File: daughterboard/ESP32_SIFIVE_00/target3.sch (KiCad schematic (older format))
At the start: 0 parts

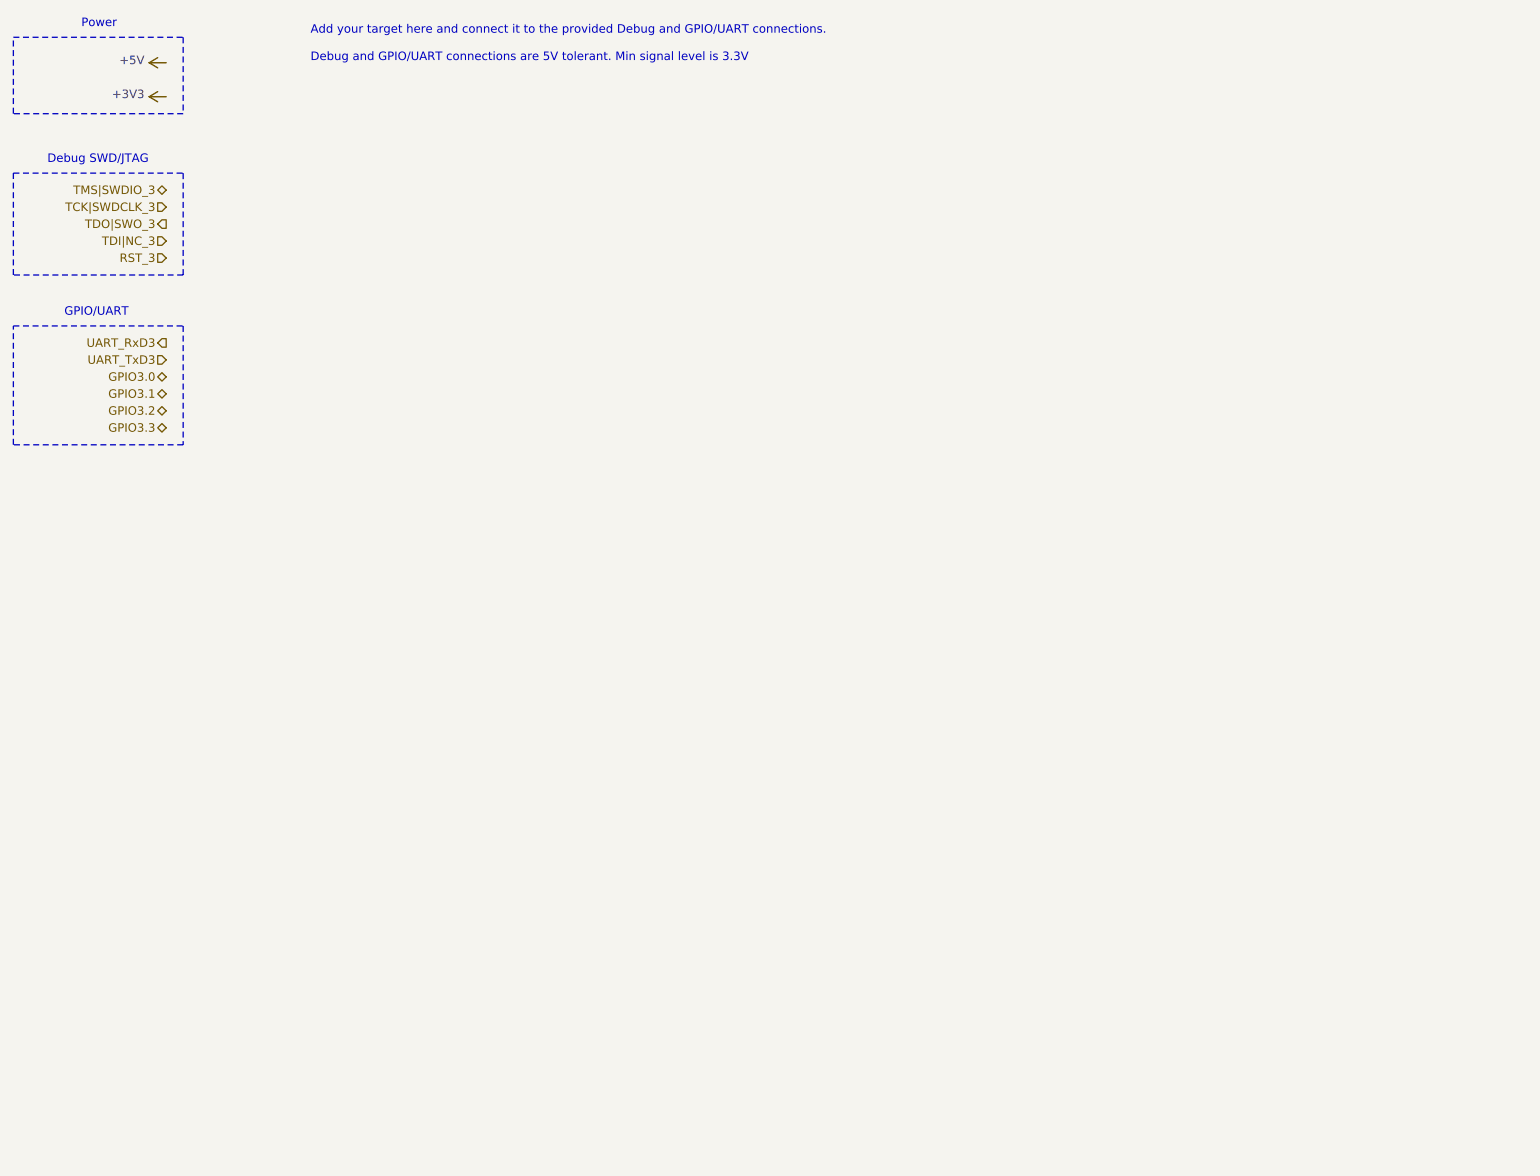
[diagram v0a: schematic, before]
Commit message: further work on ESP32/SIFIVE daughterboard
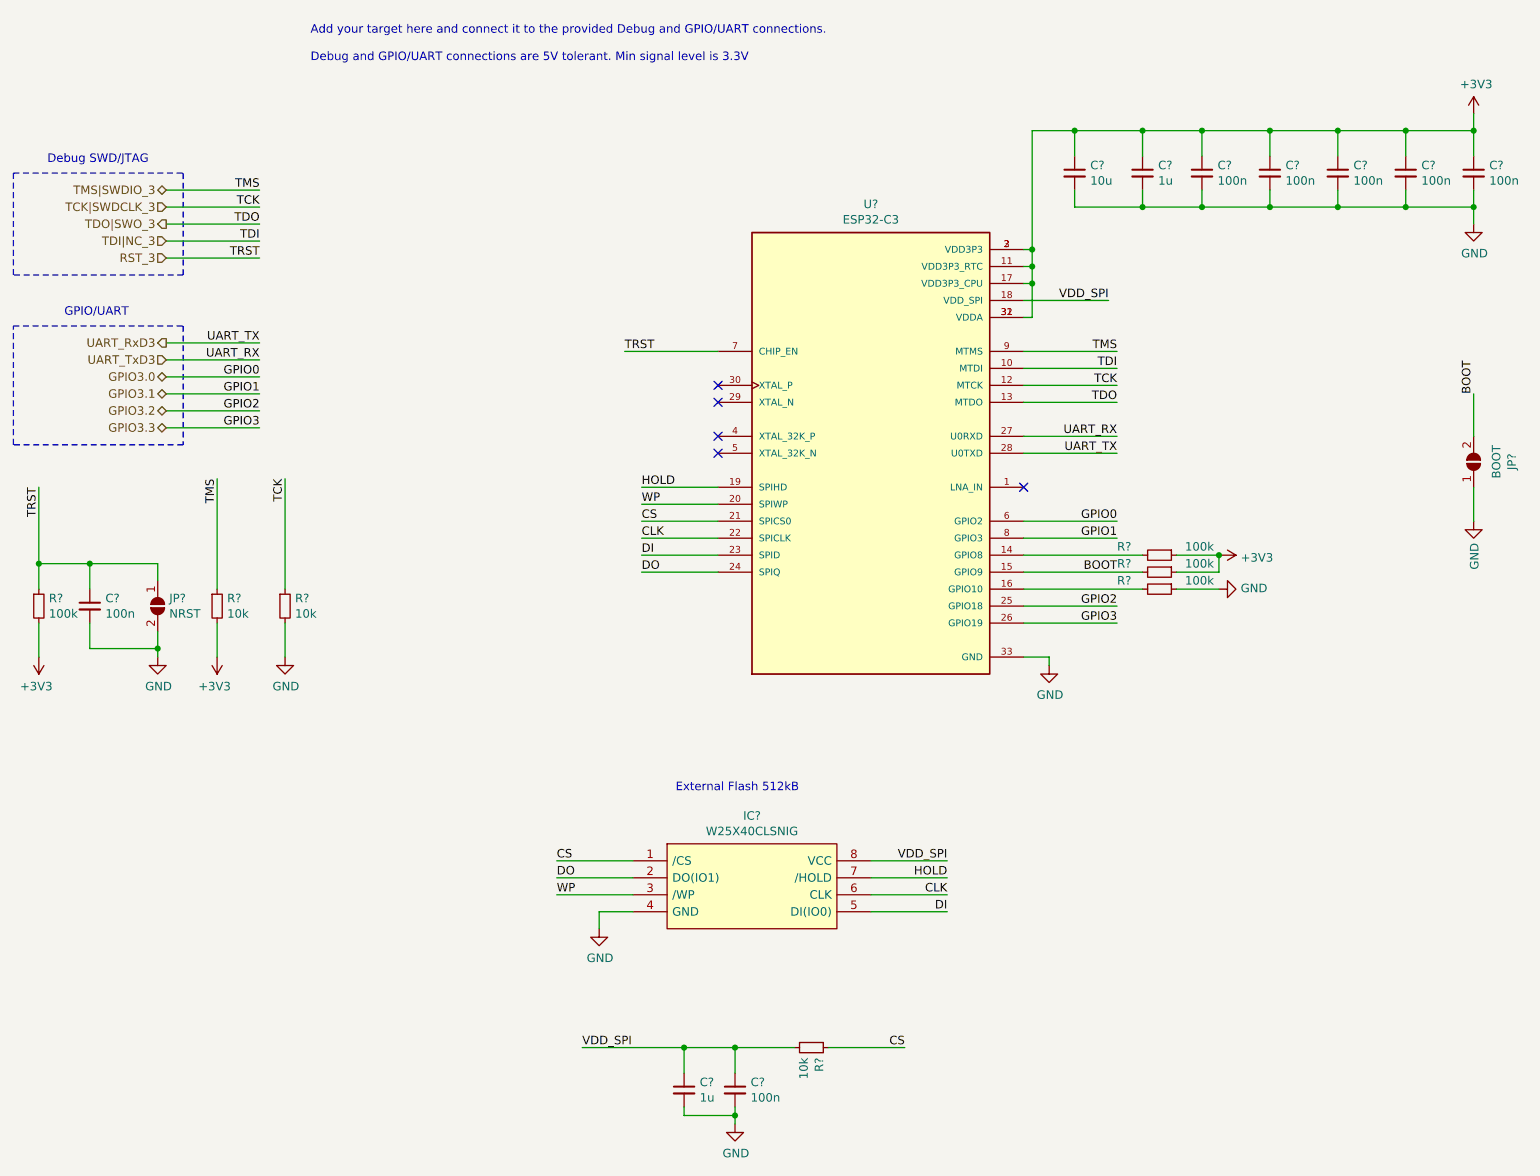
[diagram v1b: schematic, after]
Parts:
- added C? (x2): 1u, symbol Device:C_Small
- added C? (x7): 100n, symbol Device:C_Small
- added C?: 10u, symbol Device:C_Small
- added IC?: W25X40CLSNIG, hive_daughterboard:W25X40CLSNIG, symbol hive_daughterboard:W25X40CLSNIG
- added JP?: NRST, symbol Jumper:SolderJumper_2_Open
- added JP?: BOOT, symbol Jumper:SolderJumper_2_Open
- added R? (x3): 10k, symbol Device:R_Small
- added R? (x4): 100k, symbol Device:R_Small
- added U?: ESP32-C3, hive_daughterboard:ESP32-C3, symbol hive_daughterboard:ESP32-C3
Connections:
- net +3V3: now also C?.1, C?.1, C?.1, C?.1, C?.1, C?.1, C?.1, R?.1, R?.1, R?.2, R?.2, U?.11 (VDD3P3_RTC), U?.17 (VDD3P3_CPU), U?.2 (VDD3P3), U?.3 (VDD3P3), U?.31 (VDDA), U?.32 (VDDA)
- net GPIO3.0: now also U?.6 (GPIO2)
- net GPIO3.1: now also U?.8 (GPIO3)
- net GPIO3.2: now also U?.25 (GPIO18)
- net GPIO3.3: now also U?.26 (GPIO19)
- net RST_3: now also C?.1, JP?.1 (A), R?.1, U?.7 (CHIP_EN)
- net TCK|SWDCLK_3: now also R?.1, U?.12 (MTCK)
- net TDI|NC_3: now also U?.10 (MTDI)
- net TDO|SWO_3: now also U?.13 (MTDO)
- net TMS|SWDIO_3: now also R?.1, U?.9 (MTMS)
- net UART_RxD3: now also U?.28 (U0TXD)
- net UART_TxD3: now also U?.27 (U0RXD)
- new net: R?.2, U?.14 (GPIO8)
- new net: R?.2, U?.16 (GPIO10)
- new net BOOT: JP?.2 (B), R?.2, U?.15 (GPIO9)
- new net CLK: IC?.6 (CLK), U?.22 (SPICLK)
- new net CS: IC?.1 (/CS), R?.1, U?.21 (SPICS0)
- new net DI: IC?.5 (DI(IO0)), U?.23 (SPID)
- new net DO: IC?.2 (DO(IO1)), U?.24 (SPIQ)
- new net GND: C?.2, C?.2, C?.2, C?.2, C?.2, C?.2, C?.2, C?.2, C?.2, C?.2, IC?.4 (GND), JP?.1 (A), JP?.2 (B), R?.1, R?.2, U?.33 (GND)
- new net HOLD: IC?.7 (/HOLD), U?.19 (SPIHD)
- new net VDD_SPI: C?.1, C?.1, IC?.8 (VCC), R?.2, U?.18 (VDD_SPI)
- new net WP: IC?.3 (/WP), U?.20 (SPIWP)
- no-connect marks 0 -> 5
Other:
- note added: "External Flash 512kB"
- note removed: "Power"

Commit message: ERC on daughterboards
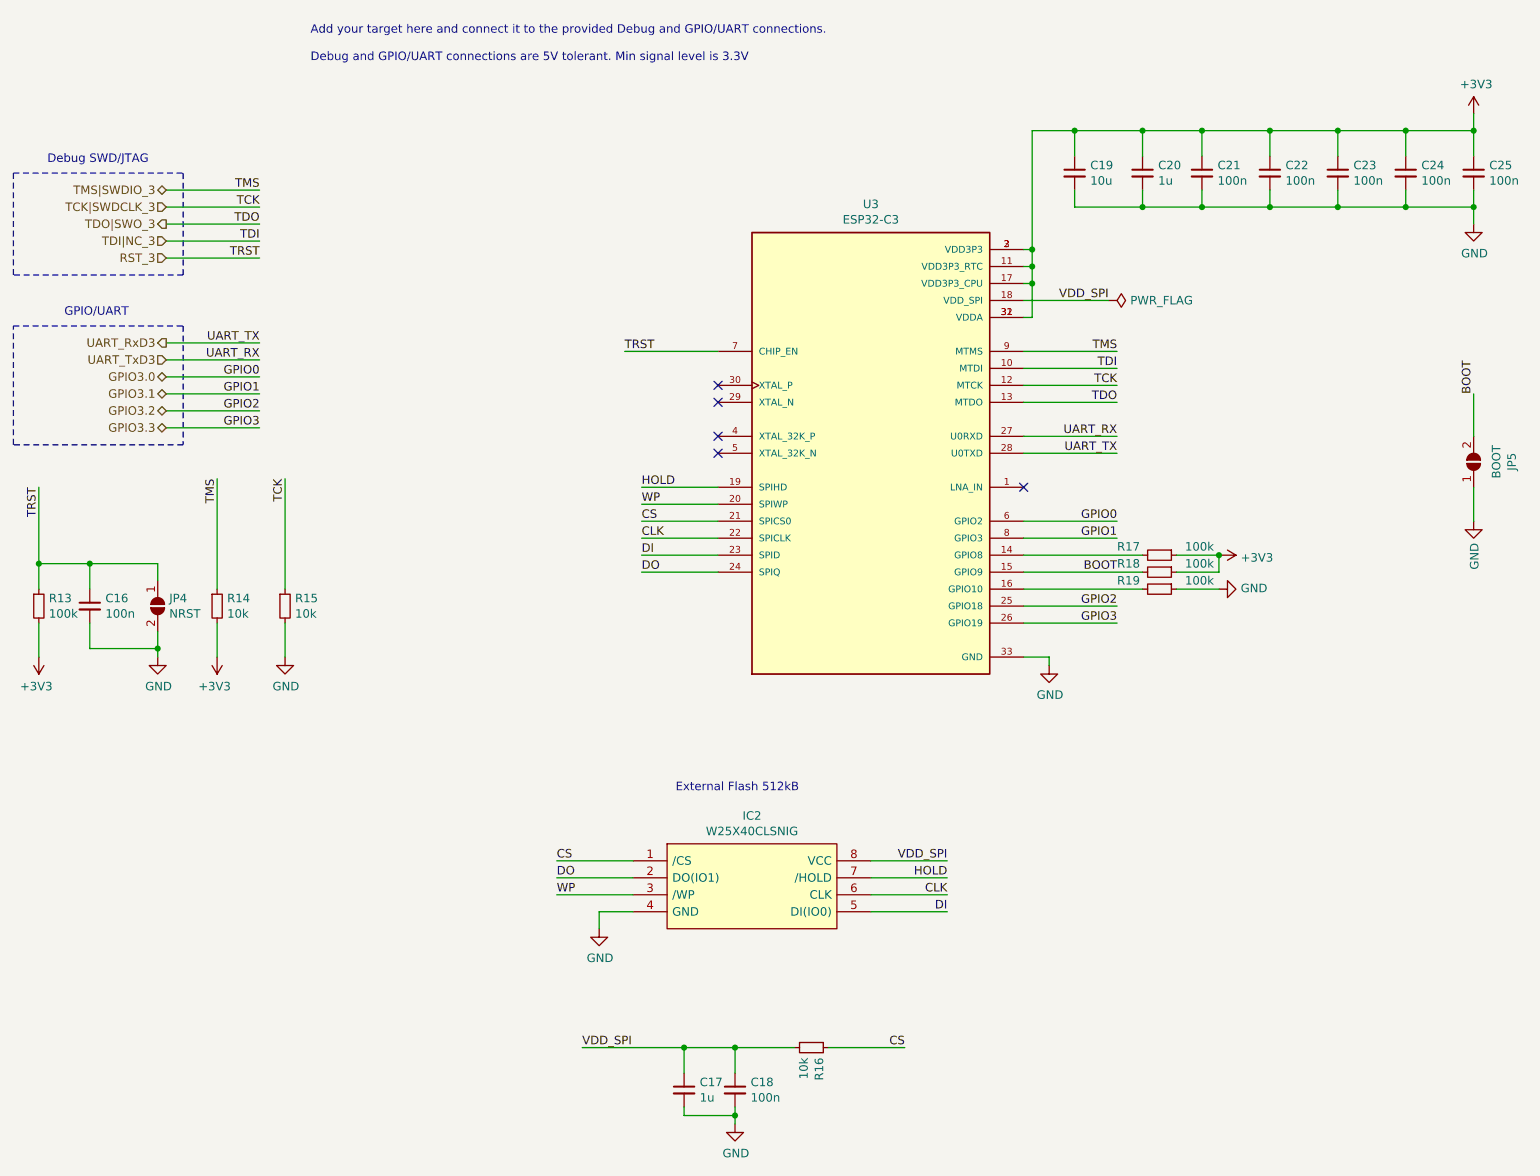
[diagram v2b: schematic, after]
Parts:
- gave numbers to parts that had none: 21
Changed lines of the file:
@@
 Add your target here and connect it to the provided Debug and GPIO/UART connections.\n\nDebug and GPIO/UART connections are 5V tolerant. Min signal level is 3.3V
 $Comp
-L hive_daughterboard:ESP32-C3 U?
+L hive_daughterboard:ESP32-C3 U3
 U 1 1 618FDF9E
 P 5800 3250
-F 0 "U?" H 5800 4717 50  0000 C CNN
+F 0 "U3" H 5800 4717 50  0000 C CNN
 F 1 "ESP32-C3" H 5800 4626 50  0000 C CNN
 F 2 "hive_daughterboard:ESP32-C3" H 5800 3250 50  0001 L BNN
@@
 $EndComp
 $Comp
-L power:GND #PWR?
+L power:GND #PWR0141
 U 1 1 61901E6F
 P 6850 4500
-F 0 "#PWR?" H 6850 4250 50  0001 C CNN
+F 0 "#PWR0141" H 6850 4250 50  0001 C CNN
 F 1 "GND" H 6855 4327 50  0000 C CNN
 F 2 "" H 6850 4500 50  0001 C CNN
@@
 WP
 $Comp
-L power:GND #PWR?
+L power:GND #PWR0142
 U 1 1 619047E6
 P 4200 6050
-F 0 "#PWR?" H 4200 5800 50  0001 C CNN
+F 0 "#PWR0142" H 4200 5800 50  0001 C CNN
 F 1 "GND" H 4205 5877 50  0000 C CNN
 F 2 "" H 4200 6050 50  0001 C CNN
@@
 External Flash 512kB
 $Comp
-L hive_daughterboard:W25X40CLSNIG IC?
+L hive_daughterboard:W25X40CLSNIG IC2
 U 1 1 6190DF80
 P 4400 5650
-F 0 "IC?" H 5100 5915 50  0000 C CNN
+F 0 "IC2" H 5100 5915 50  0000 C CNN
 F 1 "W25X40CLSNIG" H 5100 5824 50  0000 C CNN
 F 2 "hive_daughterboard:W25X40CLSNIG" H 5650 5750 50  0001 L CNN
@@
 VDD_SPI
 $Comp
-L Device:C_Small C?
+L Device:C_Small C17
 U 1 1 61910FEB
 P 4700 7000
-F 0 "C?" H 4792 7046 50  0000 L CNN
+F 0 "C17" H 4792 7046 50  0000 L CNN
 F 1 "1u" H 4792 6955 50  0000 L CNN
 F 2 "" H 4700 7000 50  0001 C CNN
@@
 $EndComp
 $Comp
-L Device:C_Small C?
+L Device:C_Small C18
 U 1 1 6191182D
 P 5000 7000
-F 0 "C?" H 5092 7046 50  0000 L CNN
+F 0 "C18" H 5092 7046 50  0000 L CNN
 F 1 "100n" H 5092 6955 50  0000 L CNN
 F 2 "" H 5000 7000 50  0001 C CNN
@@
 Connection ~ 4700 6750
 $Comp
-L power:GND #PWR?
+L power:GND #PWR0143
 U 1 1 619134B3
 P 5000 7200
-F 0 "#PWR?" H 5000 6950 50  0001 C CNN
+F 0 "#PWR0143" H 5000 6950 50  0001 C CNN
 F 1 "GND" H 5005 7027 50  0000 C CNN
 F 2 "" H 5000 7200 50  0001 C CNN
@@
 CS
 $Comp
-L Device:R_Small R?
+L Device:R_Small R16
 U 1 1 61919ECE
 P 5450 6750
-F 0 "R?" H 5509 6796 50  0000 L CNN
+F 0 "R16" H 5509 6796 50  0000 L CNN
 F 1 "10k" H 5509 6705 50  0000 L CNN
 F 2 "" H 5450 6750 50  0001 C CNN
@@
 	6750 2050 6750 1350
 $Comp
-L Device:C_Small C?
+L Device:C_Small C19
 U 1 1 619234B6
 P 7000 1600
-F 0 "C?" H 7092 1646 50  0000 L CNN
+F 0 "C19" H 7092 1646 50  0000 L CNN
 F 1 "10u" H 7092 1555 50  0000 L CNN
 F 2 "" H 7000 1600 50  0001 C CNN
@@
 Connection ~ 5000 6750
 $Comp
-L Device:C_Small C?
+L Device:C_Small C20
 U 1 1 61935CE9
 P 7400 1600
-F 0 "C?" H 7492 1646 50  0000 L CNN
+F 0 "C20" H 7492 1646 50  0000 L CNN
 F 1 "1u" H 7492 1555 50  0000 L CNN
 F 2 "" H 7400 1600 50  0001 C CNN
@@
 $EndComp
 $Comp
-L Device:C_Small C?
+L Device:C_Small C21
 U 1 1 619364E1
 P 7750 1600
-F 0 "C?" H 7842 1646 50  0000 L CNN
+F 0 "C21" H 7842 1646 50  0000 L CNN
 F 1 "100n" H 7842 1555 50  0000 L CNN
 F 2 "" H 7750 1600 50  0001 C CNN
@@
 $EndComp
 $Comp
-L Device:C_Small C?
+L Device:C_Small C22
 U 1 1 61936D2B
 P 8150 1600
-F 0 "C?" H 8242 1646 50  0000 L CNN
+F 0 "C22" H 8242 1646 50  0000 L CNN
 F 1 "100n" H 8242 1555 50  0000 L CNN
 F 2 "" H 8150 1600 50  0001 C CNN
@@
 	6750 1350 7000 1350
 $Comp
-L power:+3V3 #PWR?
+L power:+3V3 #PWR0144
 U 1 1 619393E8
 P 9350 1250
-F 0 "#PWR?" H 9350 1100 50  0001 C CNN
+F 0 "#PWR0144" H 9350 1100 50  0001 C CNN
 F 1 "+3V3" H 9365 1423 50  0000 C CNN
 F 2 "" H 9350 1250 50  0001 C CNN
@@
 	7000 1350 7400 1350
 $Comp
-L power:GND #PWR?
+L power:GND #PWR0145
 U 1 1 6193DA6B
 P 9350 1900
-F 0 "#PWR?" H 9350 1650 50  0001 C CNN
+F 0 "#PWR0145" H 9350 1650 50  0001 C CNN
 F 1 "GND" H 9355 1727 50  0000 C CNN
 F 2 "" H 9350 1900 50  0001 C CNN
@@
 Connection ~ 6750 2150
 $Comp
-L Device:C_Small C?
+L Device:C_Small C23
 U 1 1 619510B1
 P 8550 1600
-F 0 "C?" H 8642 1646 50  0000 L CNN
+F 0 "C23" H 8642 1646 50  0000 L CNN
 F 1 "100n" H 8642 1555 50  0000 L CNN
 F 2 "" H 8550 1600 50  0001 C CNN
@@
 $EndComp
 $Comp
-L Device:C_Small C?
+L Device:C_Small C24
 U 1 1 619510B7
 P 8950 1600
-F 0 "C?" H 9042 1646 50  0000 L CNN
+F 0 "C24" H 9042 1646 50  0000 L CNN
 F 1 "100n" H 9042 1555 50  0000 L CNN
 F 2 "" H 8950 1600 50  0001 C CNN
@@
 Connection ~ 6750 2250
 $Comp
-L Device:C_Small C?
+L Device:C_Small C25
 U 1 1 6195B71C
 P 9350 1600
-F 0 "C?" H 9442 1646 50  0000 L CNN
+F 0 "C25" H 9442 1646 50  0000 L CNN
 F 1 "100n" H 9442 1555 50  0000 L CNN
 F 2 "" H 9350 1600 50  0001 C CNN
@@
 P 2350 4150
 AR Path="/616688D6/6197383B" Ref="R?"  Part="1"
-AR Path="/61668157/6197383B" Ref="R?"  Part="1"
-F 0 "R?" H 2409 4196 50  0000 L CNN
+AR Path="/61668157/6197383B" Ref="R15"  Part="1"
+F 0 "R15" H 2409 4196 50  0000 L CNN
 F 1 "10k" H 2409 4105 50  0000 L CNN
 F 2 "" H 2350 4150 50  0001 C CNN
@@
 P 2350 4450
 AR Path="/616688D6/61973841" Ref="#PWR?"  Part="1"
-AR Path="/61668157/61973841" Ref="#PWR?"  Part="1"
-F 0 "#PWR?" H 2350 4200 50  0001 C CNN
+AR Path="/61668157/61973841" Ref="#PWR0146"  Part="1"
+F 0 "#PWR0146" H 2350 4200 50  0001 C CNN
 F 1 "GND" H 2355 4277 50  0000 C CNN
 F 2 "" H 2350 4450 50  0001 C CNN
@@
 P 1950 4150
 AR Path="/616688D6/61973849" Ref="R?"  Part="1"
-AR Path="/61668157/61973849" Ref="R?"  Part="1"
-F 0 "R?" H 2009 4196 50  0000 L CNN
+AR Path="/61668157/61973849" Ref="R14"  Part="1"
+F 0 "R14" H 2009 4196 50  0000 L CNN
 F 1 "10k" H 2009 4105 50  0000 L CNN
 F 2 "" H 1950 4150 50  0001 C CNN
@@
 P 1950 4450
 AR Path="/616688D6/61973851" Ref="#PWR?"  Part="1"
-AR Path="/61668157/61973851" Ref="#PWR?"  Part="1"
-F 0 "#PWR?" H 1950 4300 50  0001 C CNN
+AR Path="/61668157/61973851" Ref="#PWR0147"  Part="1"
+F 0 "#PWR0147" H 1950 4300 50  0001 C CNN
 F 1 "+3V3" H 1965 4623 50  0000 C CNN
 F 2 "" H 1950 4450 50  0001 C CNN
@@
 P 900 4150
 AR Path="/616688D6/6197C911" Ref="R?"  Part="1"
-AR Path="/61668157/6197C911" Ref="R?"  Part="1"
-F 0 "R?" H 959 4196 50  0000 L CNN
+AR Path="/61668157/6197C911" Ref="R13"  Part="1"
+F 0 "R13" H 959 4196 50  0000 L CNN
 F 1 "100k" H 959 4105 50  0000 L CNN
 F 2 "" H 900 4150 50  0001 C CNN
@@
 $EndComp
 $Comp
-L Jumper:SolderJumper_2_Open JP?
+L Jumper:SolderJumper_2_Open JP4
 U 1 1 6197D823
 P 1600 4150
-F 0 "JP?" V 1554 4218 50  0000 L CNN
+F 0 "JP4" V 1554 4218 50  0000 L CNN
 F 1 "NRST" V 1645 4218 50  0000 L CNN
 F 2 "" H 1600 4150 50  0001 C CNN
@@
 $EndComp
 $Comp
-L power:+3V3 #PWR?
+L power:+3V3 #PWR0148
 U 1 1 6197EBCD
 P 900 4450
-F 0 "#PWR?" H 900 4300 50  0001 C CNN
+F 0 "#PWR0148" H 900 4300 50  0001 C CNN
 F 1 "+3V3" H 915 4623 50  0000 C CNN
 F 2 "" H 900 4450 50  0001 C CNN
@@
 	900  3450 900  3900
 $Comp
-L power:GND #PWR?
+L power:GND #PWR0149
 U 1 1 6198A4F4
 P 1600 4450
-F 0 "#PWR?" H 1600 4200 50  0001 C CNN
+F 0 "#PWR0149" H 1600 4200 50  0001 C CNN
 F 1 "GND" H 1605 4277 50  0000 C CNN
 F 2 "" H 1600 4450 50  0001 C CNN
@@
 TRST
 $Comp
-L Device:C_Small C?
+L Device:C_Small C16
 U 1 1 61999E92
 P 1200 4150
-F 0 "C?" H 1292 4196 50  0000 L CNN
+F 0 "C16" H 1292 4196 50  0000 L CNN
 F 1 "100n" H 1292 4105 50  0000 L CNN
 F 2 "" H 1200 4150 50  0001 C CNN
@@
 GPIO3
 $Comp
-L power:GND #PWR?
+L power:GND #PWR0150
 U 1 1 619BC11C
 P 7850 4050
-F 0 "#PWR?" H 7850 3800 50  0001 C CNN
+F 0 "#PWR0150" H 7850 3800 50  0001 C CNN
 F 1 "GND" V 7855 3922 50  0000 R CNN
 F 2 "" H 7850 4050 50  0001 C CNN
@@
 	7600 4050 7850 4050
 $Comp
-L Device:R_Small R?
+L Device:R_Small R17
 U 1 1 619C3E49
 P 7500 3850
-F 0 "R?" V 7450 3600 50  0000 L CNN
+F 0 "R17" V 7450 3600 50  0000 L CNN
 F 1 "100k" V 7450 4000 50  0000 L CNN
 F 2 "" H 7500 3850 50  0001 C CNN
@@
 $EndComp
 $Comp
-L Device:R_Small R?
+L Device:R_Small R19
 U 1 1 619C4749
 P 7500 4050
-F 0 "R?" V 7450 3800 50  0000 L CNN
+F 0 "R19" V 7450 3800 50  0000 L CNN
 F 1 "100k" V 7450 4200 50  0000 L CNN
 F 2 "" H 7500 4050 50  0001 C CNN
@@
 $EndComp
 $Comp
-L Device:R_Small R?
+L Device:R_Small R18
 U 1 1 619C52BE
 P 7500 3950
-F 0 "R?" V 7450 3700 50  0000 L CNN
+F 0 "R18" V 7450 3700 50  0000 L CNN
 F 1 "100k" V 7450 4100 50  0000 L CNN
 F 2 "" H 7500 3950 50  0001 C CNN
@@
 	7400 3850 6700 3850
 $Comp
-L power:+3V3 #PWR?
+L power:+3V3 #PWR0151
 U 1 1 619C8DF3
 P 7850 3850
-F 0 "#PWR?" H 7850 3700 50  0001 C CNN
+F 0 "#PWR0151" H 7850 3700 50  0001 C CNN
 F 1 "+3V3" V 7865 3978 50  0000 L CNN
 F 2 "" H 7850 3850 50  0001 C CNN
@@
 BOOT
 $Comp
-L Jumper:SolderJumper_2_Open JP?
+L Jumper:SolderJumper_2_Open JP5
 U 1 1 619F39F3
 P 9350 3300
-F 0 "JP?" H 9350 3075 50  0000 C CNN
+F 0 "JP5" H 9350 3075 50  0000 C CNN
 F 1 "BOOT" H 9350 3166 50  0000 C CNN
 F 2 "" H 9350 3300 50  0001 C CNN
@@
 $EndComp
 $Comp
-L power:GND #PWR?
+L power:GND #PWR0152
 U 1 1 619F6187
 P 9350 3650
-F 0 "#PWR?" H 9350 3400 50  0001 C CNN
+F 0 "#PWR0152" H 9350 3400 50  0001 C CNN
 F 1 "GND" V 9355 3522 50  0000 R CNN
 F 2 "" H 9350 3650 50  0001 C CNN
@@
 NoConn ~ 4900 3150
 NoConn ~ 4900 3250
+$Comp
+L power:PWR_FLAG #FLG0102
+U 1 1 619000D0
+P 7200 2350
+F 0 "#FLG0102" H 7200 2425 50  0001 C CNN
+F 1 "PWR_FLAG" V 7200 2478 50  0000 L CNN
+F 2 "" H 7200 2350 50  0001 C CNN
+F 3 "~" H 7200 2350 50  0001 C CNN
+	1    7200 2350
+	0    1    1    0
+$EndComp
 $EndSCHEMATC
